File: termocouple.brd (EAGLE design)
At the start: 69.8 x 100 mm, 19 parts, among them IC1 MAX6675, IC2 MAX6675, IC3 MAX6675, IC4 MAX6675, U2 TC1262_VDB, X2 1751248, X3 1751248, X4 1751248, X5 1751248

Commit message: brd
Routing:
- net +12V: track 5.74 -> 16.8 mm
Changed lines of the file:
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@@
 <wire x1="10.7188" y1="31.9786" x2="10.29" y2="31.9786" width="0.8128" layer="1"/>
 <wire x1="10.29" y1="31.9786" x2="10.29" y2="26.67" width="0.8128" layer="1"/>
+<wire x1="16.51" y1="36.83" x2="13.97" y2="36.83" width="0.6096" layer="1"/>
+<wire x1="13.97" y1="36.83" x2="13.97" y2="31.75" width="0.6096" layer="1"/>
+<wire x1="13.97" y1="31.75" x2="10.7188" y2="31.75" width="0.6096" layer="1"/>
+<wire x1="10.7188" y1="31.75" x2="10.7188" y2="31.9786" width="0.6096" layer="1"/>
 <wire x1="10.16" y1="49.378" x2="62.23" y2="69.85" width="0" layer="19" extent="1-1"/>
-<wire x1="16.51" y1="36.83" x2="10.16" y2="49.378" width="0" layer="19" extent="1-1"/>
-<wire x1="10.7188" y1="31.9786" x2="16.51" y2="36.83" width="0" layer="19" extent="1-1"/>
+<wire x1="13.97" y1="36.83" x2="10.16" y2="49.378" width="0" layer="19" extent="1-1"/>
 </signal>
 <signal name="N$64">

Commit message: brd
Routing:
- net N$5: track 0.00 -> 55.2 mm
- net N$8: track 0.00 -> 50.9 mm
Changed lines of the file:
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@@
 <contactref element="U$1" pad="SDA"/>
 <contactref element="X1" pad="3"/>
-<wire x1="16.51" y1="41.91" x2="25.4" y2="87.63" width="0" layer="19" extent="1-1"/>
+<wire x1="16.51" y1="41.91" x2="15.24" y2="41.91" width="0.4064" layer="1"/>
+<wire x1="15.24" y1="41.91" x2="13.97" y2="43.18" width="0.4064" layer="1"/>
+<wire x1="13.97" y1="43.18" x2="13.97" y2="46.99" width="0.4064" layer="1"/>
+<wire x1="13.97" y1="46.99" x2="16.51" y2="49.53" width="0.4064" layer="1"/>
+<wire x1="16.51" y1="49.53" x2="21.59" y2="49.53" width="0.4064" layer="1"/>
+<wire x1="21.59" y1="49.53" x2="22.86" y2="50.8" width="0.4064" layer="1"/>
+<wire x1="22.86" y1="50.8" x2="22.86" y2="82.55" width="0.4064" layer="1"/>
+<wire x1="22.86" y1="82.55" x2="25.4" y2="85.09" width="0.4064" layer="1"/>
+<wire x1="25.4" y1="85.09" x2="25.4" y2="87.63" width="0.4064" layer="1"/>
 </signal>
 <signal name="N$8">
 <contactref element="U$1" pad="SCL"/>
 <contactref element="X1" pad="4"/>
-<wire x1="16.51" y1="44.45" x2="27.94" y2="87.63" width="0" layer="19" extent="1-1"/>
+<wire x1="27.94" y1="87.63" x2="27.94" y2="83.82" width="0.4064" layer="1"/>
+<wire x1="27.94" y1="83.82" x2="24.13" y2="80.01" width="0.4064" layer="1"/>
+<wire x1="24.13" y1="80.01" x2="24.13" y2="49.53" width="0.4064" layer="1"/>
+<wire x1="24.13" y1="49.53" x2="22.86" y2="48.26" width="0.4064" layer="1"/>
+<wire x1="22.86" y1="48.26" x2="17.78" y2="48.26" width="0.4064" layer="1"/>
+<wire x1="17.78" y1="48.26" x2="16.51" y2="46.99" width="0.4064" layer="1"/>
+<wire x1="16.51" y1="46.99" x2="16.51" y2="44.45" width="0.4064" layer="1"/>
 </signal>
 <signal name="N$9">

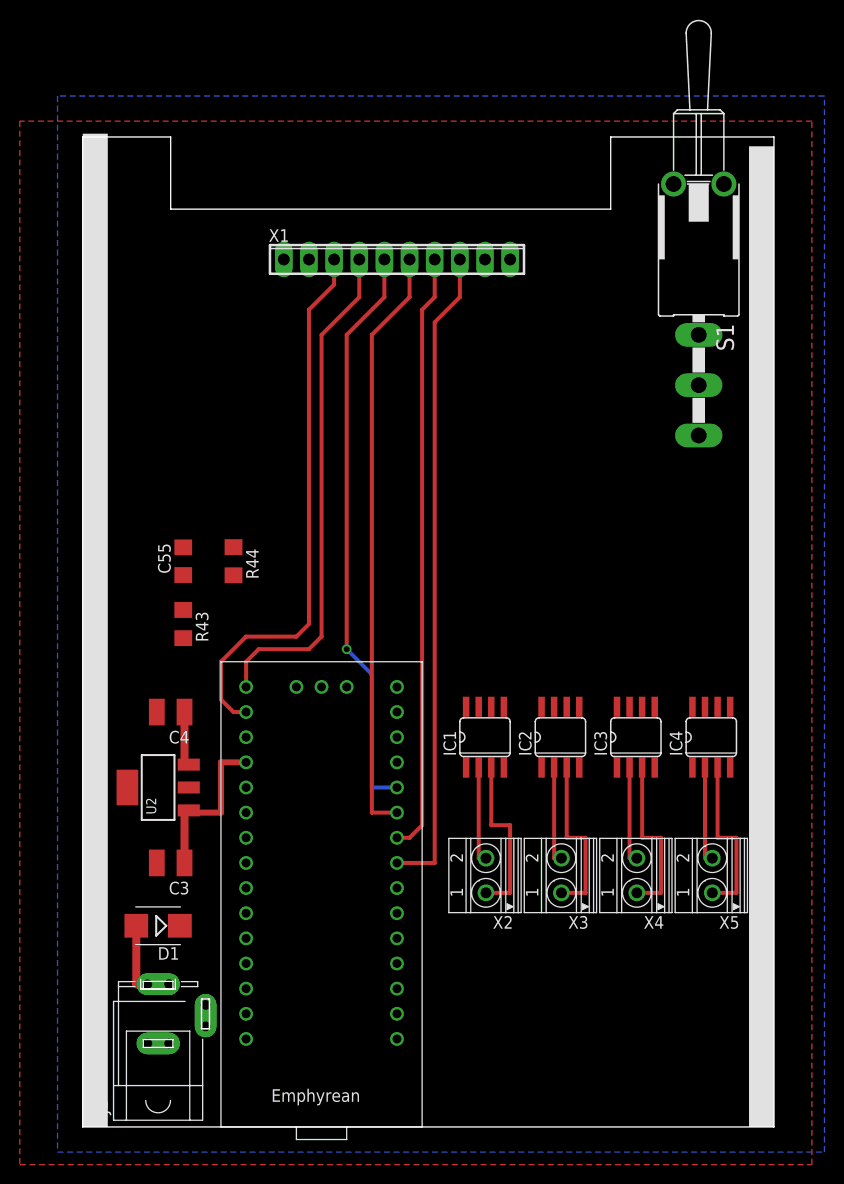
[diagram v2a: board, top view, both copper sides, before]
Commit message: brd
power supply measuring, should do somthing with the rest of the adc pins?
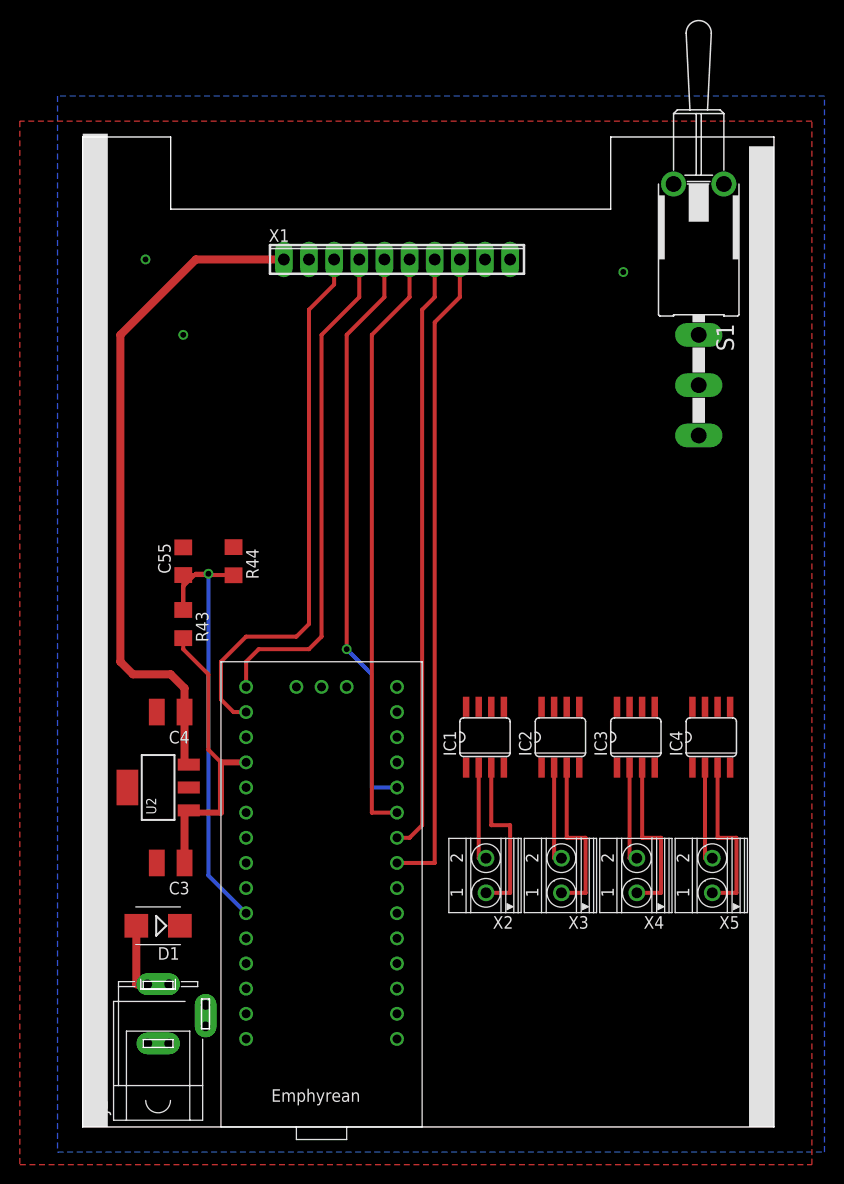
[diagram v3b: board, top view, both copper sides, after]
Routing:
- net +3V3: track 5.74 -> 68.4 mm
- net N$64: track 0.00 -> 49.9 mm, vias 0 -> 1
- net +12V: track 16.8 -> 31.0 mm
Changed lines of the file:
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@@
 <wire x1="10.7188" y1="36.6014" x2="10.29" y2="36.6014" width="0.8128" layer="1"/>
 <wire x1="10.29" y1="36.6014" x2="10.29" y2="41.91" width="0.8128" layer="1"/>
-<wire x1="10.29" y1="41.91" x2="20.32" y2="87.63" width="0" layer="19" extent="1-1"/>
-<wire x1="42.545" y1="36.2966" x2="10.7188" y2="36.6014" width="0" layer="19" extent="1-1"/>
-<wire x1="50.165" y1="36.2966" x2="42.545" y2="36.2966" width="0" layer="19" extent="1-1"/>
-<wire x1="57.785" y1="36.2966" x2="50.165" y2="36.2966" width="0" layer="19" extent="1-1"/>
-<wire x1="65.405" y1="36.2966" x2="57.785" y2="36.2966" width="0" layer="19" extent="1-1"/>
+<wire x1="10.29" y1="41.91" x2="10.29" y2="44.32" width="0.8128" layer="1"/>
+<wire x1="10.29" y1="44.32" x2="8.89" y2="45.72" width="0.8128" layer="1"/>
+<wire x1="8.89" y1="45.72" x2="5.08" y2="45.72" width="0.8128" layer="1"/>
+<wire x1="5.08" y1="45.72" x2="3.81" y2="46.99" width="0.8128" layer="1"/>
+<wire x1="3.81" y1="46.99" x2="3.81" y2="80.01" width="0.8128" layer="1"/>
+<wire x1="3.81" y1="80.01" x2="11.43" y2="87.63" width="0.8128" layer="1"/>
+<wire x1="11.43" y1="87.63" x2="20.32" y2="87.63" width="0.8128" layer="1"/>
+<wire x1="57.785" y1="36.2966" x2="65.405" y2="36.2966" width="0" layer="19" extent="1-1"/>
+<wire x1="50.165" y1="36.2966" x2="57.785" y2="36.2966" width="0" layer="19" extent="1-1"/>
+<wire x1="42.545" y1="36.2966" x2="50.165" y2="36.2966" width="0" layer="19" extent="1-1"/>
+<wire x1="10.7188" y1="36.6014" x2="42.545" y2="36.2966" width="0" layer="19" extent="1-1"/>
 </signal>
 <signal name="GND">
@@
 <vertex x="-6.35" y="101.6"/>
 </polygon>
+<via x="6.35" y="87.63" extent="1-16" drill="0.6" shape="square"/>
+<via x="10.16" y="80.01" extent="1-16" drill="0.6" shape="square"/>
+<via x="54.61" y="86.36" extent="1-16" drill="0.6" shape="square"/>
 </signal>
 <signal name="N$4">
@@
 <wire x1="13.97" y1="31.75" x2="10.7188" y2="31.75" width="0.6096" layer="1"/>
 <wire x1="10.7188" y1="31.75" x2="10.7188" y2="31.9786" width="0.6096" layer="1"/>
-<wire x1="10.16" y1="49.378" x2="62.23" y2="69.85" width="0" layer="19" extent="1-1"/>
-<wire x1="13.97" y1="36.83" x2="10.16" y2="49.378" width="0" layer="19" extent="1-1"/>
+<wire x1="10.16" y1="49.378" x2="10.16" y2="48.26" width="0.4064" layer="1"/>
+<wire x1="10.16" y1="48.26" x2="12.7" y2="45.72" width="0.4064" layer="1"/>
+<wire x1="12.7" y1="45.72" x2="12.7" y2="38.1" width="0.4064" layer="1"/>
+<wire x1="12.7" y1="38.1" x2="13.97" y2="36.83" width="0.4064" layer="1"/>
+<wire x1="12.7" y1="45.72" x2="62.23" y2="69.85" width="0" layer="19" extent="1-1"/>
 </signal>
 <signal name="N$64">
@@
 <contactref element="C55" pad="1"/>
 <contactref element="U$1" pad="A2"/>
-<wire x1="10.16" y1="55.75" x2="15.24" y2="55.728" width="0" layer="19" extent="1-1"/>
-<wire x1="10.16" y1="52.222" x2="10.16" y2="55.75" width="0" layer="19" extent="1-1"/>
-<wire x1="16.51" y1="21.59" x2="10.16" y2="52.222" width="0" layer="19" extent="1-1"/>
+<wire x1="10.16" y1="52.222" x2="10.16" y2="55.75" width="0.4064" layer="1"/>
+<wire x1="10.16" y1="55.75" x2="15.218" y2="55.75" width="0.4064" layer="1"/>
+<wire x1="15.218" y1="55.75" x2="15.24" y2="55.728" width="0.4064" layer="1"/>
+<wire x1="10.16" y1="52.222" x2="10.16" y2="54.61" width="0.4064" layer="1"/>
+<wire x1="10.16" y1="54.61" x2="11.43" y2="55.88" width="0.4064" layer="1"/>
+<wire x1="11.43" y1="55.88" x2="12.7" y2="55.88" width="0.4064" layer="1"/>
+<via x="12.7" y="55.88" extent="1-16" drill="0.6" shape="square"/>
+<wire x1="12.7" y1="55.88" x2="12.7" y2="25.4" width="0.4064" layer="16"/>
+<wire x1="12.7" y1="25.4" x2="16.51" y2="21.59" width="0.4064" layer="16"/>
 </signal>
 <signal name="N$5">
